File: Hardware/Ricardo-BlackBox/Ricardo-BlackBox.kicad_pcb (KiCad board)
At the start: 4 copper layers, 45.1 x 35.1 mm, 83 parts, among them J1 RBUS, J2 USB_C_Receptacle_USB2.0, J3 Conn_01x08_Pin, U1 ESP32-S3, U2 SN65HVD230, U3 LM66200DRLR, U4 MAX77827AEFD+T, U5 SC4215ASTRT, U7 LM66200DRLR, Y1 R940000171

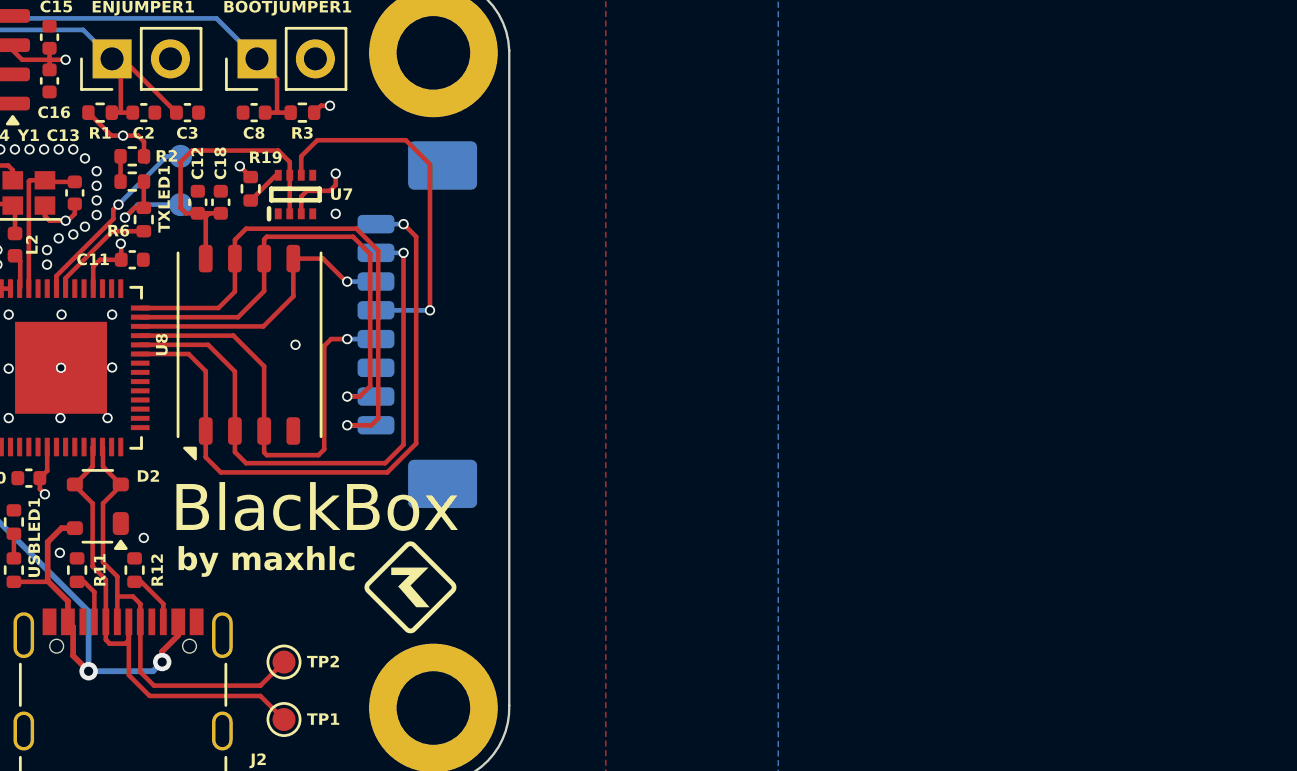
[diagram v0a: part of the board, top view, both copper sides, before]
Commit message: Changed to PicoClasp connector
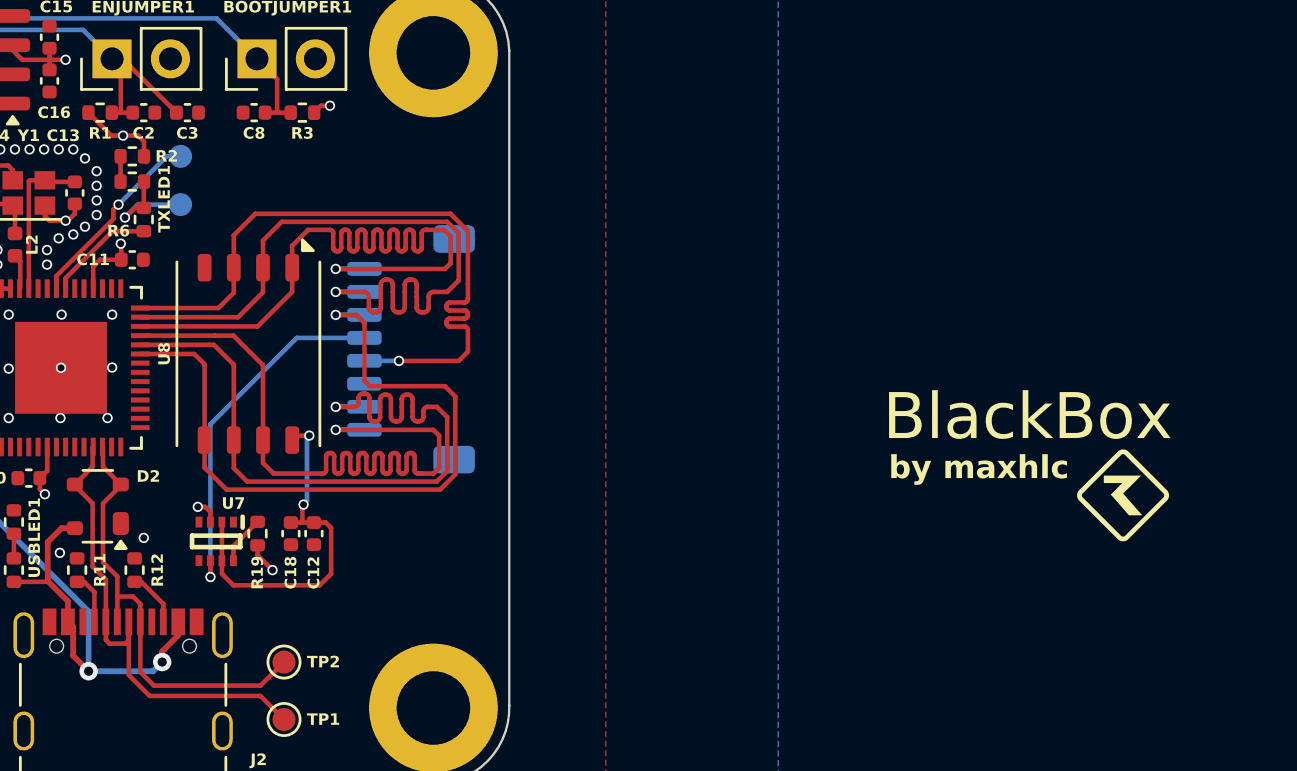
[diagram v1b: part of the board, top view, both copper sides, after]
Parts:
- J3: footprint Connector_Molex:Molex_PicoBlade_53261-0871_1x08-1MP_P1.25mm_Horizontal -> Connector_Molex:Molex_Pico-Clasp_202396-0807_1x08-1MP_P1.00mm_Horizontal
- moved G*** 31.3 mm to (150.9, 68.3)
- moved U7 15.5 mm to (111.5, 70.3), turned to -90 degrees
- moved C12 15.3 mm to (115.7, 70.0), turned to -90 degrees
- moved R19 15.0 mm to (113.3, 70.0), turned to -90 degrees
- moved C18 14.7 mm to (114.7, 70.0), turned to -90 degrees
- moved J3 1.38 mm to (120.0, 62.0)
- moved U8 0.40 mm to (112.9, 62.2), turned to -90 degrees
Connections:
- U1 pad 37: /NAND_SD2 -> /NAND_CMD
- U1 pad 38: /NAND_SD3 -> /NAND_SD0
- U1 pad 39: /NAND_CLK -> /NAND_SD1
- U1 pad 40: /NAND_CMD -> /NAND_SD2
- U1 pad 41: /NAND_SD0 -> /NAND_SD3
- U1 pad 42: /NAND_SD1 -> /NAND_CLK
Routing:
- net /NAND_CMD: track 12.9 -> 31.8 mm
- net /NAND_SD0: track 21.3 -> 33.1 mm
- net /NAND_CLK: track 19.3 -> 30.8 mm
- net /NAND_SD1: track 23.5 -> 34.4 mm
- net /NAND_SD3: track 25.5 -> 32.2 mm
- net /NAND_SD2: track 27.8 -> 33.6 mm
- net /NAND_3V3: track 13.3 -> 16.0 mm, vias 0 -> 2
- net +3V3: track 31.4 -> 30.2 mm
- net Net-(U7-ST): track 1.55 -> 2.12 mm
- net GND: vias 53 -> 51
